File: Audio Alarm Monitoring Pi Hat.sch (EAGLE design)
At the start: 7 parts, among them J1 35RAPC4BHN2, J2 2X6 FEMALE

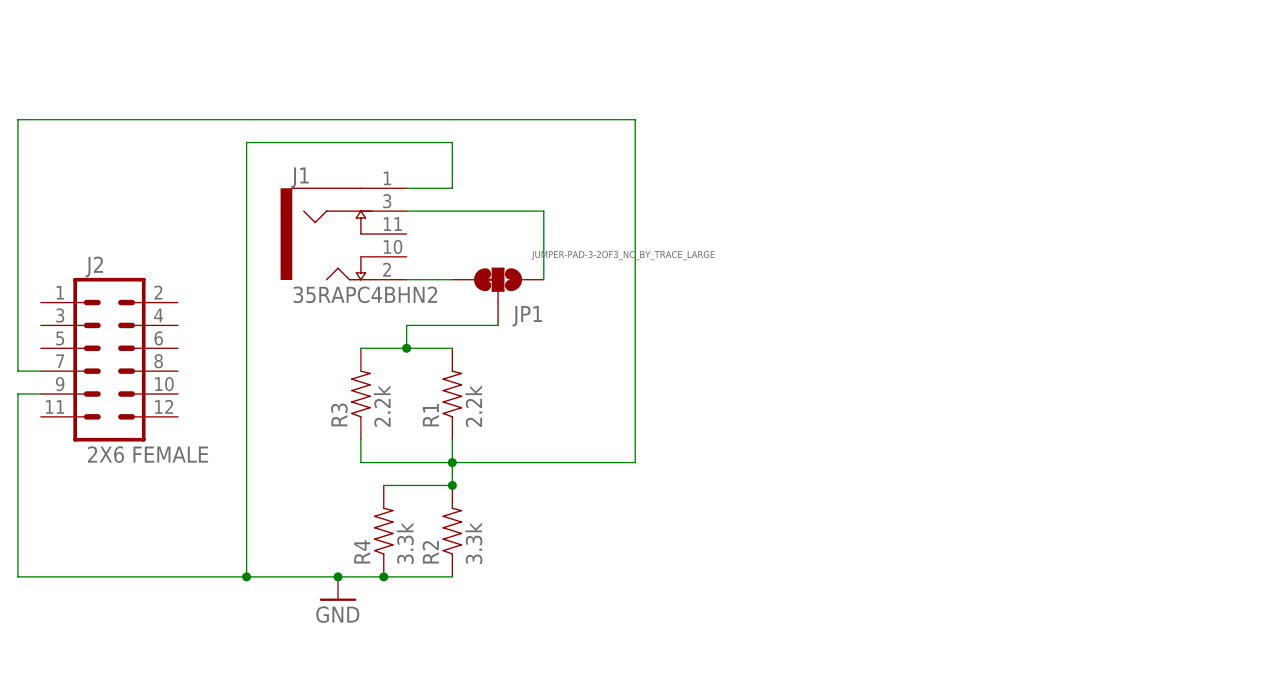
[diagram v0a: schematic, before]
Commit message: Updating for LED + all surface mount resistors
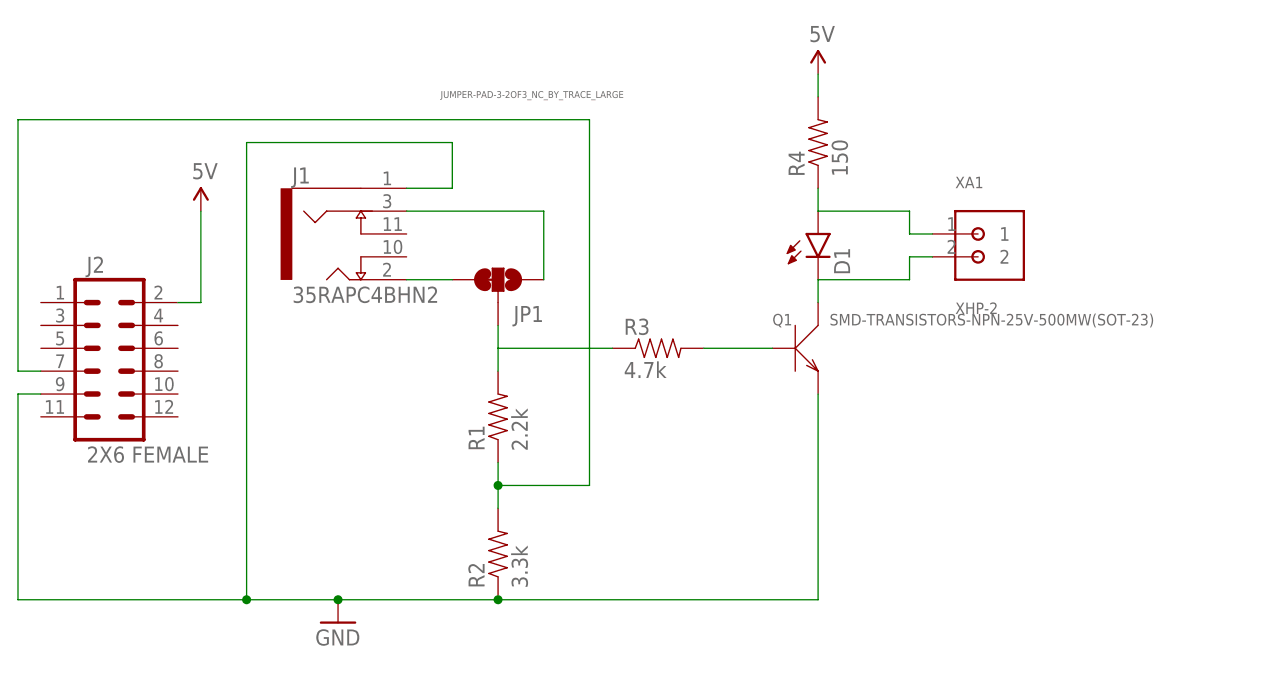
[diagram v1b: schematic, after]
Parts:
- added D1: (no value), SparkFun-LED:LED1206
- added Q1: SMD-TRANSISTORS-NPN-25V-500MW(SOT-23), SMD-TRANSISTORS-NPN-25V-500MW_SOT-23_:SMD-TRANSISTORS-NPN-25V-500MW(SOT-23)
- added XA1: XHP-2, XHP-2:XHP-2
- R1, R2: device SparkFun-Resistors:RESISTORPTH-1/4W -> SparkFun-Passives:RESISTOR1206
- R3: value 2.2k -> 4.7k; device SparkFun-Passives:RESISTOR0805-RES -> SparkFun-Passives:RESISTOR1206
- R4: value 3.3k -> 150; device SparkFun-Passives:RESISTOR0805-RES -> SparkFun-Passives:RESISTOR1206
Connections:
- new net 5V: J2.2, R4.2
- new net N$5: D1.C, Q1.C, XA1.2
- new net N$8: D1.A, R4.1, XA1.1
- new net N$9: Q1.B, R3.2
- net GND: now also Q1.E; no longer R4.1
- net N$1: no longer R3.1, R4.2
- net N$2: now also R3.1; no longer R3.2
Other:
- moved on the sheet: R1, R2, R3, R4
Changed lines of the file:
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@@
 <parts>
 <part name="J1" library="35RAPC4BHN2" deviceset="35RAPC4BHN2" device=""/>
-<part name="R1" library="SparkFun-Resistors" deviceset="RESISTOR" device="PTH-1/4W" value="2.2k"/>
-<part name="R2" library="SparkFun-Resistors" deviceset="RESISTOR" device="PTH-1/4W" value="3.3k"/>
 <part name="GND1" library="SparkFun-Aesthetics" deviceset="GND" device=""/>
 <part name="J2" library="SparkFun-Connectors" deviceset="M06X2" device="PTH_FEMALE" value="2X6 FEMALE"/>
-<part name="R3" library="SparkFun-Passives" deviceset="RESISTOR" device="0805-RES" value="2.2k"/>
-<part name="R4" library="SparkFun-Passives" deviceset="RESISTOR" device="0805-RES" value="3.3k"/>
 <part name="JP1" library="SparkFun-Passives" deviceset="JUMPER-PAD-3-2OF3_NC_BY_TRACE" device="_LARGE"/>
+<part name="D1" library="SparkFun-LED" deviceset="LED" device="1206"/>
+<part name="R1" library="SparkFun-Passives" deviceset="RESISTOR" device="1206" value="2.2k"/>
+<part name="R2" library="SparkFun-Passives" deviceset="RESISTOR" device="1206" value="3.3k"/>
+<part name="R4" library="SparkFun-Passives" deviceset="RESISTOR" device="1206" value="150"/>
+<part name="R3" library="SparkFun-Passives" deviceset="RESISTOR" device="1206" value="4.7k"/>
+<part name="Q1" library="SMD-TRANSISTORS-NPN-25V-500MW_SOT-23_" deviceset="SMD-TRANSISTORS-NPN-25V-500MW(SOT-23)" device=""/>
+<part name="SUPPLY1" library="SparkFun-Aesthetics" deviceset="5V" device=""/>
+<part name="SUPPLY2" library="SparkFun-Aesthetics" deviceset="5V" device=""/>
+<part name="XA1" library="XHP-2" deviceset="XHP-2" device=""/>
 </parts>
 <sheets>
@@
 <instances>
 <instance part="J1" gate="G$1" x="73.66" y="68.58"/>
-<instance part="R1" gate="G$1" x="86.36" y="50.8" rot="R90"/>
-<instance part="R2" gate="G$1" x="86.36" y="35.56" rot="R90"/>
-<instance part="GND1" gate="1" x="73.66" y="27.94"/>
+<instance part="GND1" gate="1" x="73.66" y="25.4"/>
 <instance part="J2" gate="G$1" x="45.72" y="48.26"/>
-<instance part="R3" gate="G$1" x="76.2" y="50.8" rot="R90"/>
-<instance part="R4" gate="G$1" x="78.74" y="35.56" rot="R90"/>
 <instance part="JP1" gate="G$1" x="91.44" y="63.5" smashed="yes" rot="MR90">
 <attribute name="NAME" x="96.52" y="58.801" size="1.778" layer="95" rot="MR0"/>
-<attribute name="VALUE" x="115.57" y="65.913" size="0.762" layer="96" rot="MR0"/>
+<attribute name="VALUE" x="105.41" y="83.693" size="0.762" layer="96" rot="MR0"/>
 </instance>
+<instance part="D1" gate="G$1" x="127" y="68.58"/>
+<instance part="R1" gate="G$1" x="91.44" y="48.26" rot="R90"/>
+<instance part="R2" gate="G$1" x="91.44" y="33.02" rot="R90"/>
+<instance part="R4" gate="G$1" x="127" y="78.74" rot="R90"/>
+<instance part="R3" gate="G$1" x="109.22" y="55.88"/>
+<instance part="Q1" gate="G$1" x="124.46" y="55.88"/>
+<instance part="SUPPLY1" gate="G$1" x="58.42" y="71.12"/>
+<instance part="SUPPLY2" gate="G$1" x="127" y="86.36"/>
+<instance part="XA1" gate="G$1" x="144.78" y="68.58"/>
 </instances>
 <busses>
@@
 <net name="N$1" class="0">
 <segment>
-<pinref part="R1" gate="G$1" pin="1"/>
-<pinref part="R2" gate="G$1" pin="2"/>
-<wire x1="86.36" y1="40.64" x2="86.36" y2="43.18" width="0.1524" layer="91"/>
-<wire x1="86.36" y1="43.18" x2="86.36" y2="45.72" width="0.1524" layer="91"/>
-<wire x1="86.36" y1="43.18" x2="106.68" y2="43.18" width="0.1524" layer="91"/>
-<junction x="86.36" y="43.18"/>
-<wire x1="106.68" y1="43.18" x2="106.68" y2="81.28" width="0.1524" layer="91"/>
-<wire x1="106.68" y1="81.28" x2="38.1" y2="81.28" width="0.1524" layer="91"/>
+<wire x1="91.44" y1="38.1" x2="91.44" y2="40.64" width="0.1524" layer="91"/>
+<wire x1="91.44" y1="40.64" x2="101.6" y2="40.64" width="0.1524" layer="91"/>
+<junction x="91.44" y="40.64"/>
+<wire x1="101.6" y1="40.64" x2="101.6" y2="81.28" width="0.1524" layer="91"/>
+<wire x1="101.6" y1="81.28" x2="38.1" y2="81.28" width="0.1524" layer="91"/>
 <wire x1="38.1" y1="81.28" x2="38.1" y2="53.34" width="0.1524" layer="91"/>
 <pinref part="J2" gate="G$1" pin="7"/>
 <wire x1="38.1" y1="53.34" x2="40.64" y2="53.34" width="0.1524" layer="91"/>
-<pinref part="R3" gate="G$1" pin="1"/>
-<wire x1="86.36" y1="43.18" x2="76.2" y2="43.18" width="0.1524" layer="91"/>
-<wire x1="76.2" y1="43.18" x2="76.2" y2="45.72" width="0.1524" layer="91"/>
-<pinref part="R4" gate="G$1" pin="2"/>
-<wire x1="78.74" y1="40.64" x2="86.36" y2="40.64" width="0.1524" layer="91"/>
-<junction x="86.36" y="40.64"/>
+<wire x1="91.44" y1="40.64" x2="91.44" y2="43.18" width="0.1524" layer="91"/>
+<pinref part="R1" gate="G$1" pin="1"/>
+<pinref part="R2" gate="G$1" pin="2"/>
 </segment>
 </net>
 <net name="GND" class="0">
 <segment>
-<pinref part="R2" gate="G$1" pin="1"/>
 <pinref part="GND1" gate="1" pin="GND"/>
-<wire x1="73.66" y1="30.48" x2="78.74" y2="30.48" width="0.1524" layer="91"/>
-<junction x="73.66" y="30.48"/>
-<wire x1="78.74" y1="30.48" x2="86.36" y2="30.48" width="0.1524" layer="91"/>
-<wire x1="73.66" y1="30.48" x2="63.5" y2="30.48" width="0.1524" layer="91"/>
+<junction x="73.66" y="27.94"/>
+<wire x1="73.66" y1="27.94" x2="91.44" y2="27.94" width="0.1524" layer="91"/>
+<wire x1="73.66" y1="27.94" x2="63.5" y2="27.94" width="0.1524" layer="91"/>
 <wire x1="63.5" y1="78.74" x2="86.36" y2="78.74" width="0.1524" layer="91"/>
 <wire x1="86.36" y1="78.74" x2="86.36" y2="73.66" width="0.1524" layer="91"/>
 <pinref part="J1" gate="G$1" pin="1"/>
 <wire x1="86.36" y1="73.66" x2="81.28" y2="73.66" width="0.1524" layer="91"/>
-<wire x1="63.5" y1="30.48" x2="63.5" y2="78.74" width="0.1524" layer="91"/>
+<wire x1="63.5" y1="27.94" x2="63.5" y2="78.74" width="0.1524" layer="91"/>
 <pinref part="J2" gate="G$1" pin="9"/>
 <wire x1="40.64" y1="50.8" x2="38.1" y2="50.8" width="0.1524" layer="91"/>
-<wire x1="38.1" y1="50.8" x2="38.1" y2="30.48" width="0.1524" layer="91"/>
-<wire x1="38.1" y1="30.48" x2="63.5" y2="30.48" width="0.1524" layer="91"/>
-<junction x="63.5" y="30.48"/>
-<pinref part="R4" gate="G$1" pin="1"/>
-<junction x="78.74" y="30.48"/>
+<wire x1="38.1" y1="50.8" x2="38.1" y2="27.94" width="0.1524" layer="91"/>
+<wire x1="38.1" y1="27.94" x2="63.5" y2="27.94" width="0.1524" layer="91"/>
+<junction x="63.5" y="27.94"/>
+<pinref part="R2" gate="G$1" pin="1"/>
+<junction x="91.44" y="27.94"/>
+<pinref part="Q1" gate="G$1" pin="E"/>
+<wire x1="127" y1="50.8" x2="127" y2="27.94" width="0.1524" layer="91"/>
+<wire x1="127" y1="27.94" x2="91.44" y2="27.94" width="0.1524" layer="91"/>
 </segment>
 </net>
 <net name="N$2" class="0">
 <segment>
+<pinref part="JP1" gate="G$1" pin="2"/>
+<wire x1="91.44" y1="58.42" x2="91.44" y2="55.88" width="0.1524" layer="91"/>
 <pinref part="R1" gate="G$1" pin="2"/>
-<pinref part="R3" gate="G$1" pin="2"/>
-<wire x1="76.2" y1="55.88" x2="81.28" y2="55.88" width="0.1524" layer="91"/>
-<pinref part="JP1" gate="G$1" pin="2"/>
-<wire x1="81.28" y1="55.88" x2="86.36" y2="55.88" width="0.1524" layer="91"/>
-<wire x1="91.44" y1="58.42" x2="81.28" y2="58.42" width="0.1524" layer="91"/>
-<wire x1="81.28" y1="58.42" x2="81.28" y2="55.88" width="0.1524" layer="91"/>
-<junction x="81.28" y="55.88"/>
+<pinref part="R3" gate="G$1" pin="1"/>
+<wire x1="91.44" y1="55.88" x2="91.44" y2="53.34" width="0.1524" layer="91"/>
+<wire x1="104.14" y1="55.88" x2="91.44" y2="55.88" width="0.1524" layer="91"/>
 </segment>
 </net>
@@
 <segment>
 <pinref part="JP1" gate="G$1" pin="1"/>
+<pinref part="J1" gate="G$1" pin="3"/>
 <wire x1="96.52" y1="63.5" x2="96.52" y2="71.12" width="0.1524" layer="91"/>
-<pinref part="J1" gate="G$1" pin="3"/>
 <wire x1="96.52" y1="71.12" x2="81.28" y2="71.12" width="0.1524" layer="91"/>
 </segment>
 </net>
+<net name="5V" class="0">
+<segment>
+<pinref part="J2" gate="G$1" pin="2"/>
+<pinref part="SUPPLY1" gate="G$1" pin="5V"/>
+<wire x1="55.88" y1="60.96" x2="58.42" y2="60.96" width="0.1524" layer="91"/>
+<wire x1="58.42" y1="60.96" x2="58.42" y2="71.12" width="0.1524" layer="91"/>
+</segment>
+<segment>
+<pinref part="SUPPLY2" gate="G$1" pin="5V"/>
+<pinref part="R4" gate="G$1" pin="2"/>
+<wire x1="127" y1="86.36" x2="127" y2="83.82" width="0.1524" layer="91"/>
+</segment>
+</net>
+<net name="N$5" class="0">
+<segment>
+<pinref part="D1" gate="G$1" pin="C"/>
+<pinref part="Q1" gate="G$1" pin="C"/>
+<wire x1="127" y1="63.5" x2="127" y2="60.96" width="0.1524" layer="91"/>
+<wire x1="127" y1="63.5" x2="137.16" y2="63.5" width="0.1524" layer="91"/>
+<wire x1="137.16" y1="63.5" x2="137.16" y2="66.04" width="0.1524" layer="91"/>
+<pinref part="XA1" gate="G$1" pin="2"/>
+<wire x1="137.16" y1="66.04" x2="139.7" y2="66.04" width="0.1524" layer="91"/>
+</segment>
+</net>
+<net name="N$8" class="0">
+<segment>
+<pinref part="R4" gate="G$1" pin="1"/>
+<pinref part="D1" gate="G$1" pin="A"/>
+<wire x1="127" y1="73.66" x2="127" y2="71.12" width="0.1524" layer="91"/>
+<wire x1="127" y1="71.12" x2="137.16" y2="71.12" width="0.1524" layer="91"/>
+<wire x1="137.16" y1="71.12" x2="137.16" y2="68.58" width="0.1524" layer="91"/>
+<pinref part="XA1" gate="G$1" pin="1"/>
+<wire x1="137.16" y1="68.58" x2="139.7" y2="68.58" width="0.1524" layer="91"/>
+</segment>
+</net>
+<net name="N$9" class="0">
+<segment>
+<pinref part="R3" gate="G$1" pin="2"/>
+<pinref part="Q1" gate="G$1" pin="B"/>
+<wire x1="114.3" y1="55.88" x2="121.92" y2="55.88" width="0.1524" layer="91"/>
+</segment>
+</net>
